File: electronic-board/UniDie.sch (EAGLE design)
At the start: 27 parts, among them IC1 ATMEGA88-THIN, J1 PJ-037A, J2 AVR_SPI_PROG_3X2NS

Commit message: Update on schematic and board.
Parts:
- removed R1, R10, R11, R13, R2, R3, R4, R6, R9: 120ohm, fab:RES-US1206FAB
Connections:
- removed net N$13: 7-SEG-LED2.5-DP, R6.2
- removed net N$2: 7-SEG-LED1.1-E, R3.2
- removed net N$3: 7-SEG-LED1.2-D, R4.2
- removed net N$4: 7-SEG-LED1.4-C, R1.2
- removed net N$5: 7-SEG-LED1.5-DP, R2.2
- removed net N$6: 7-SEG-LED1.10-G, R9.1
- removed net N$7: 7-SEG-LED1.9-F, R11.1
- removed net N$8: 7-SEG-LED1.7-A, R10.1
- removed net N$9: 7-SEG-LED1.6-B, R13.1
- removed net TA: R10.2
- removed net TB: R13.2
- removed net TC: R1.1
- removed net TD: R4.1
- removed net TDP: R2.1
- removed net TE: R3.1
- removed net TF: R11.2
- removed net TG: R9.2
- removed net UA: R16.2
- removed net UB: R17.2
- removed net UC: R5.1
- removed net UD: R8.1
- removed net UDP: R6.1
- removed net UE: R7.1
- removed net UF: R12.2
- removed net UG: R15.2
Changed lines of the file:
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@@
 <part name="SUPPLY5" library="SparkFun-PowerSymbols" deviceset="5V" device=""/>
 <part name="GND5" library="SparkFun-PowerSymbols" deviceset="GND" device=""/>
-<part name="R1" library="fab" deviceset="RES-US" device="1206FAB" value="120ohm"/>
-<part name="R2" library="fab" deviceset="RES-US" device="1206FAB" value="120ohm"/>
-<part name="R3" library="fab" deviceset="RES-US" device="1206FAB" value="120ohm"/>
-<part name="R4" library="fab" deviceset="RES-US" device="1206FAB" value="120ohm"/>
 <part name="R5" library="fab" deviceset="RES-US" device="1206FAB" value="120ohm"/>
-<part name="R6" library="fab" deviceset="RES-US" device="1206FAB" value="120ohm"/>
 <part name="R7" library="fab" deviceset="RES-US" device="1206FAB" value="120ohm"/>
 <part name="R8" library="fab" deviceset="RES-US" device="1206FAB" value="120ohm"/>
-<part name="R9" library="fab" deviceset="RES-US" device="1206FAB" value="120ohm"/>
-<part name="R10" library="fab" deviceset="RES-US" device="1206FAB" value="120ohm"/>
-<part name="R11" library="fab" deviceset="RES-US" device="1206FAB" value="120ohm"/>
 <part name="R12" library="fab" deviceset="RES-US" device="1206FAB" value="120ohm"/>
-<part name="R13" library="fab" deviceset="RES-US" device="1206FAB" value="120ohm"/>
 <part name="R15" library="fab" deviceset="RES-US" device="1206FAB" value="120ohm"/>
 <part name="R16" library="fab" deviceset="RES-US" device="1206FAB" value="120ohm"/>
@@
 <instance part="SUPPLY5" gate="G$1" x="78.74" y="40.64"/>
 <instance part="GND5" gate="1" x="190.5" y="5.08"/>
-<instance part="R1" gate="G$1" x="22.86" y="33.02"/>
-<instance part="R2" gate="G$1" x="22.86" y="25.4"/>
-<instance part="R3" gate="G$1" x="22.86" y="45.72"/>
-<instance part="R4" gate="G$1" x="22.86" y="38.1"/>
 <instance part="R5" gate="G$1" x="22.86" y="2.54"/>
-<instance part="R6" gate="G$1" x="22.86" y="-5.08"/>
 <instance part="R7" gate="G$1" x="22.86" y="15.24"/>
 <instance part="R8" gate="G$1" x="22.86" y="7.62"/>
-<instance part="R9" gate="G$1" x="63.5" y="45.72"/>
-<instance part="R10" gate="G$1" x="63.5" y="33.02"/>
-<instance part="R11" gate="G$1" x="63.5" y="38.1"/>
 <instance part="R12" gate="G$1" x="63.5" y="7.62"/>
-<instance part="R13" gate="G$1" x="63.5" y="25.4"/>
 <instance part="R15" gate="G$1" x="63.5" y="15.24"/>
 <instance part="R16" gate="G$1" x="63.5" y="2.54"/>
@@
 </segment>
 </net>
-<net name="N$2" class="0">
-<segment>
-<pinref part="R3" gate="G$1" pin="2"/>
-<wire x1="27.94" y1="45.72" x2="30.48" y2="45.72" width="0.1524" layer="91"/>
-<wire x1="30.48" y1="45.72" x2="30.48" y2="40.64" width="0.1524" layer="91"/>
-<pinref part="7-SEG-LED1" gate="G$1" pin="1-E"/>
-<wire x1="30.48" y1="40.64" x2="33.02" y2="40.64" width="0.1524" layer="91"/>
-</segment>
-</net>
-<net name="N$3" class="0">
-<segment>
-<pinref part="7-SEG-LED1" gate="G$1" pin="2-D"/>
-<pinref part="R4" gate="G$1" pin="2"/>
-<wire x1="33.02" y1="38.1" x2="27.94" y2="38.1" width="0.1524" layer="91"/>
-</segment>
-</net>
-<net name="N$4" class="0">
-<segment>
-<pinref part="7-SEG-LED1" gate="G$1" pin="4-C"/>
-<pinref part="R1" gate="G$1" pin="2"/>
-<wire x1="33.02" y1="33.02" x2="27.94" y2="33.02" width="0.1524" layer="91"/>
-</segment>
-</net>
-<net name="N$5" class="0">
-<segment>
-<pinref part="7-SEG-LED1" gate="G$1" pin="5-DP"/>
-<wire x1="33.02" y1="30.48" x2="30.48" y2="30.48" width="0.1524" layer="91"/>
-<wire x1="30.48" y1="30.48" x2="30.48" y2="25.4" width="0.1524" layer="91"/>
-<pinref part="R2" gate="G$1" pin="2"/>
-<wire x1="30.48" y1="25.4" x2="27.94" y2="25.4" width="0.1524" layer="91"/>
-</segment>
-</net>
-<net name="N$6" class="0">
-<segment>
-<pinref part="7-SEG-LED1" gate="G$1" pin="10-G"/>
-<wire x1="53.34" y1="40.64" x2="55.88" y2="40.64" width="0.1524" layer="91"/>
-<wire x1="55.88" y1="40.64" x2="55.88" y2="45.72" width="0.1524" layer="91"/>
-<pinref part="R9" gate="G$1" pin="1"/>
-<wire x1="55.88" y1="45.72" x2="58.42" y2="45.72" width="0.1524" layer="91"/>
-</segment>
-</net>
-<net name="N$7" class="0">
-<segment>
-<pinref part="7-SEG-LED1" gate="G$1" pin="9-F"/>
-<pinref part="R11" gate="G$1" pin="1"/>
-<wire x1="53.34" y1="38.1" x2="58.42" y2="38.1" width="0.1524" layer="91"/>
-</segment>
-</net>
-<net name="N$8" class="0">
-<segment>
-<pinref part="7-SEG-LED1" gate="G$1" pin="7-A"/>
-<pinref part="R10" gate="G$1" pin="1"/>
-<wire x1="53.34" y1="33.02" x2="58.42" y2="33.02" width="0.1524" layer="91"/>
-</segment>
-</net>
-<net name="N$9" class="0">
-<segment>
-<pinref part="7-SEG-LED1" gate="G$1" pin="6-B"/>
-<wire x1="53.34" y1="30.48" x2="55.88" y2="30.48" width="0.1524" layer="91"/>
-<wire x1="55.88" y1="30.48" x2="55.88" y2="25.4" width="0.1524" layer="91"/>
-<pinref part="R13" gate="G$1" pin="1"/>
-<wire x1="55.88" y1="25.4" x2="58.42" y2="25.4" width="0.1524" layer="91"/>
-</segment>
-</net>
 <net name="N$10" class="0">
 <segment>
@@
 </segment>
 </net>
-<net name="N$13" class="0">
-<segment>
-<pinref part="7-SEG-LED2" gate="G$1" pin="5-DP"/>
-<wire x1="33.02" y1="0" x2="30.48" y2="0" width="0.1524" layer="91"/>
-<wire x1="30.48" y1="0" x2="30.48" y2="-2.54" width="0.1524" layer="91"/>
-<pinref part="R6" gate="G$1" pin="2"/>
-<wire x1="30.48" y1="-2.54" x2="30.48" y2="-5.08" width="0.1524" layer="91"/>
-<wire x1="30.48" y1="-5.08" x2="27.94" y2="-5.08" width="0.1524" layer="91"/>
-</segment>
-</net>
-<net name="TE" class="0">
-<segment>
-<pinref part="R3" gate="G$1" pin="1"/>
-<wire x1="17.78" y1="45.72" x2="15.24" y2="45.72" width="0.1524" layer="91"/>
-<label x="15.24" y="48.26" size="1.778" layer="95" rot="R180"/>
-</segment>
-</net>
-<net name="TD" class="0">
-<segment>
-<pinref part="R4" gate="G$1" pin="1"/>
-<wire x1="17.78" y1="38.1" x2="15.24" y2="38.1" width="0.1524" layer="91"/>
-<label x="15.24" y="40.64" size="1.778" layer="95" rot="R180"/>
-</segment>
-</net>
-<net name="TC" class="0">
-<segment>
-<pinref part="R1" gate="G$1" pin="1"/>
-<wire x1="17.78" y1="33.02" x2="15.24" y2="33.02" width="0.1524" layer="91"/>
-<label x="15.24" y="35.56" size="1.778" layer="95" rot="R180"/>
-</segment>
-</net>
-<net name="TDP" class="0">
-<segment>
-<pinref part="R2" gate="G$1" pin="1"/>
-<wire x1="17.78" y1="25.4" x2="15.24" y2="25.4" width="0.1524" layer="91"/>
-<label x="15.24" y="27.94" size="1.778" layer="95" rot="R180"/>
-</segment>
-</net>
-<net name="TG" class="0">
-<segment>
-<pinref part="R9" gate="G$1" pin="2"/>
-<wire x1="68.58" y1="45.72" x2="71.12" y2="45.72" width="0.1524" layer="91"/>
-<label x="71.12" y="45.72" size="1.778" layer="95"/>
-</segment>
-</net>
-<net name="TF" class="0">
-<segment>
-<pinref part="R11" gate="G$1" pin="2"/>
-<wire x1="68.58" y1="38.1" x2="71.12" y2="38.1" width="0.1524" layer="91"/>
-<label x="71.12" y="38.1" size="1.778" layer="95"/>
-</segment>
-</net>
-<net name="TA" class="0">
-<segment>
-<pinref part="R10" gate="G$1" pin="2"/>
-<wire x1="68.58" y1="33.02" x2="71.12" y2="33.02" width="0.1524" layer="91"/>
-<label x="71.12" y="33.02" size="1.778" layer="95"/>
-</segment>
-</net>
-<net name="TB" class="0">
-<segment>
-<pinref part="R13" gate="G$1" pin="2"/>
-<wire x1="68.58" y1="25.4" x2="71.12" y2="25.4" width="0.1524" layer="91"/>
-<label x="71.12" y="25.4" size="1.778" layer="95"/>
-</segment>
-</net>
-<net name="UE" class="0">
-<segment>
-<pinref part="R7" gate="G$1" pin="1"/>
-<wire x1="17.78" y1="15.24" x2="15.24" y2="15.24" width="0.1524" layer="91"/>
-<label x="15.24" y="17.78" size="1.778" layer="95" rot="R180"/>
-</segment>
-</net>
-<net name="UD" class="0">
-<segment>
-<pinref part="R8" gate="G$1" pin="1"/>
-<wire x1="17.78" y1="7.62" x2="15.24" y2="7.62" width="0.1524" layer="91"/>
-<label x="15.24" y="10.16" size="1.778" layer="95" rot="R180"/>
-</segment>
-</net>
-<net name="UC" class="0">
-<segment>
-<pinref part="R5" gate="G$1" pin="1"/>
-<wire x1="17.78" y1="2.54" x2="15.24" y2="2.54" width="0.1524" layer="91"/>
-<label x="15.24" y="5.08" size="1.778" layer="95" rot="R180"/>
-</segment>
-</net>
-<net name="UDP" class="0">
-<segment>
-<pinref part="R6" gate="G$1" pin="1"/>
-<wire x1="17.78" y1="-5.08" x2="15.24" y2="-5.08" width="0.1524" layer="91"/>
-<label x="15.24" y="-2.54" size="1.778" layer="95" rot="R180"/>
-</segment>
-</net>
-<net name="UG" class="0">
-<segment>
-<pinref part="R15" gate="G$1" pin="2"/>
-<wire x1="68.58" y1="15.24" x2="71.12" y2="15.24" width="0.1524" layer="91"/>
-<label x="71.12" y="15.24" size="1.778" layer="95"/>
-</segment>
-</net>
 <net name="N$27" class="0">
 <segment>
@@
 </segment>
 </net>
-<net name="UF" class="0">
-<segment>
-<pinref part="R12" gate="G$1" pin="2"/>
-<wire x1="68.58" y1="7.62" x2="71.12" y2="7.62" width="0.1524" layer="91"/>
-<label x="71.12" y="7.62" size="1.778" layer="95"/>
-</segment>
-</net>
-<net name="UA" class="0">
-<segment>
-<pinref part="R16" gate="G$1" pin="2"/>
-<wire x1="68.58" y1="2.54" x2="71.12" y2="2.54" width="0.1524" layer="91"/>
-<label x="71.12" y="2.54" size="1.778" layer="95"/>
-</segment>
-</net>
-<net name="UB" class="0">
-<segment>
-<pinref part="R17" gate="G$1" pin="2"/>
-<wire x1="68.58" y1="-5.08" x2="71.12" y2="-5.08" width="0.1524" layer="91"/>
-<label x="71.12" y="-5.08" size="1.778" layer="95"/>
-</segment>
-</net>

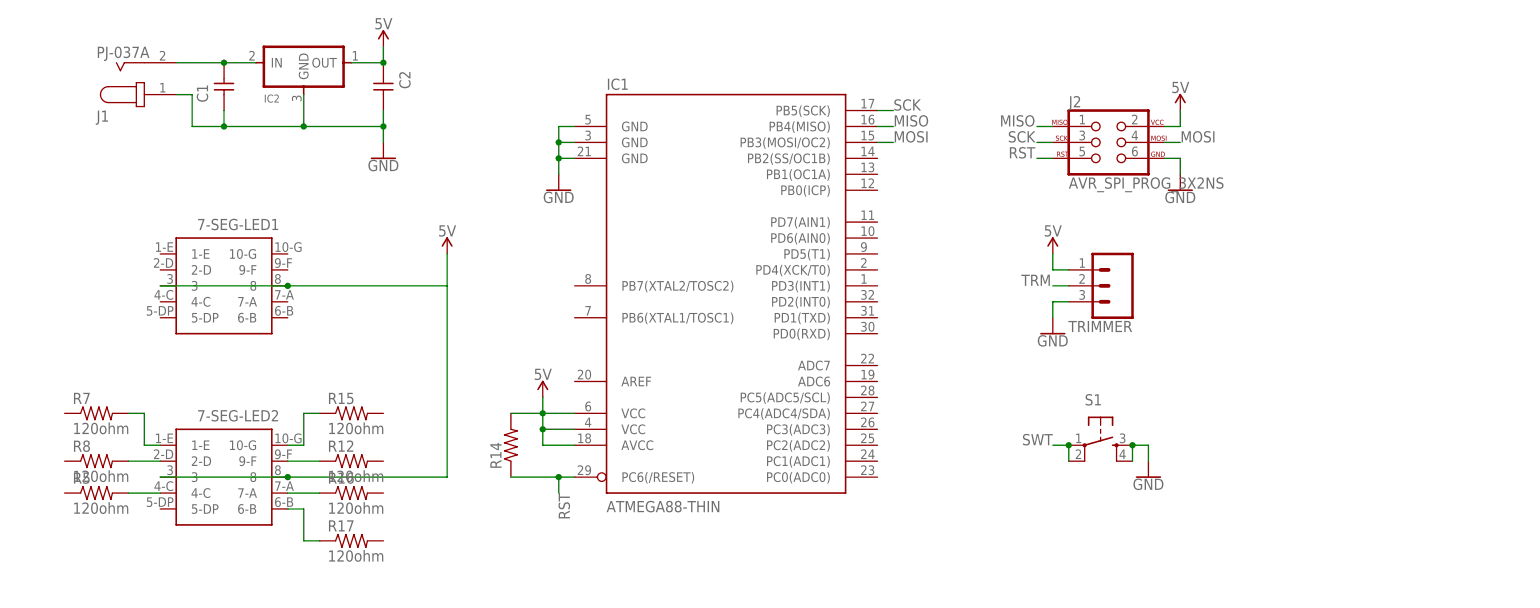
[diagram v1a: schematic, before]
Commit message: Finished schematic and approximate board layout. Updated electronics BOM
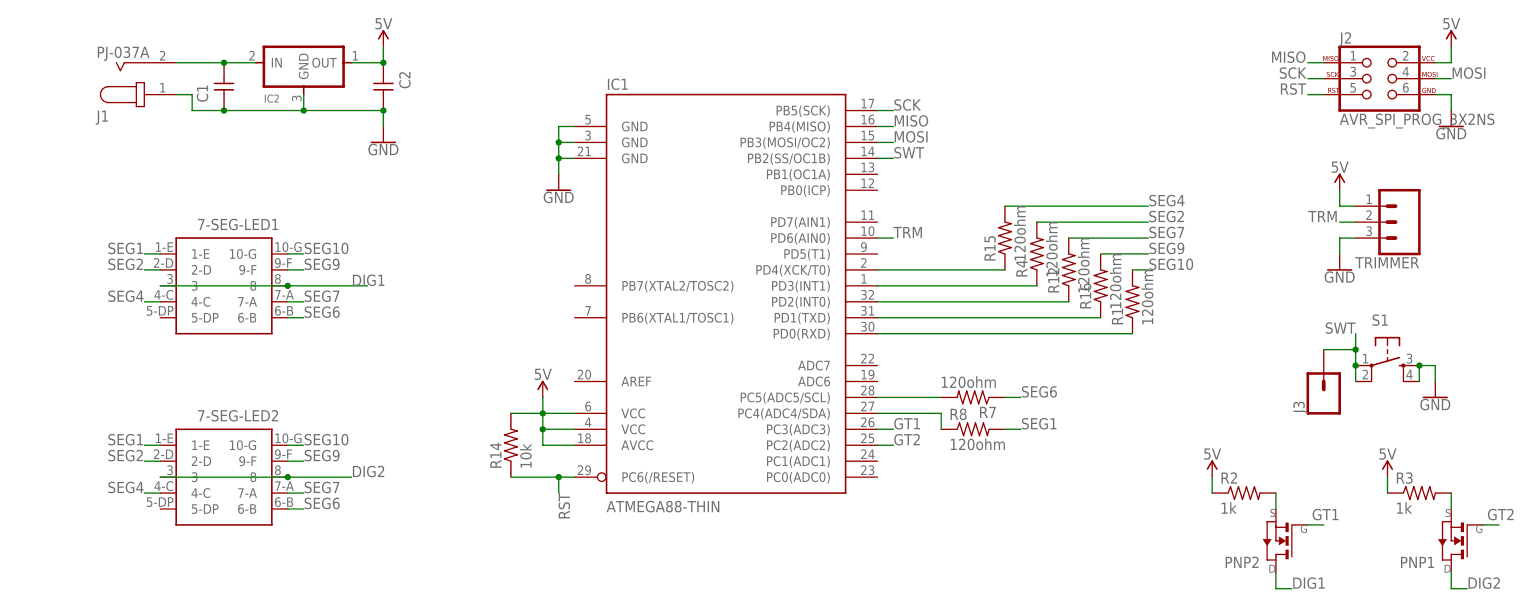
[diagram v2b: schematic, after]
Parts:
- removed R17, R5: 120ohm, fab:RES-US1206FAB
- added J3: (no value), SparkFun-Connectors:CONN_01PTH_NO_SILK_YES_STOP
- added PNP1, PNP2: (no value), fab:NMOSFETSOT23
- added R1, R4: 120ohm, fab:RES-US1206FAB
- added R2, R3: 1k, fab:RES-US1206FAB
- R14: value (none) -> 10k
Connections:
- removed net N$11: 7-SEG-LED2.2-D, R8.2
- removed net N$12: 7-SEG-LED2.4-C, R5.2
- removed net N$27: 7-SEG-LED2.10-G, R15.1
- removed net N$28: 7-SEG-LED2.9-F, R12.1
- removed net N$29: 7-SEG-LED2.7-A, R16.1
- removed net N$30: 7-SEG-LED2.6-B, R17.1
- new net DIG1: 7-SEG-LED1.3, 7-SEG-LED1.8, PNP2.D
- new net DIG2: 7-SEG-LED2.3, 7-SEG-LED2.8, PNP1.D
- new net GT1: IC1.PC3(ADC3), PNP2.G
- new net GT2: IC1.PC2(ADC2), PNP1.G
- new net N$13: PNP2.S, R2.2
- new net N$2: PNP1.S, R3.2
- new net N$3: IC1.PC5(ADC5/SCL), R7.2
- new net N$4: IC1.PC4(ADC4/SDA), R8.1
- new net N$6: IC1.PD4(XCK/T0), R15.1
- new net N$7: IC1.PD3(INT1), R4.1
- new net N$8: IC1.PD2(INT0), R12.1
- new net N$9: IC1.PD1(TXD), R16.1
- new net SEG1: 7-SEG-LED1.1-E, 7-SEG-LED2.1-E, R8.2
- new net SEG10: 7-SEG-LED1.10-G, 7-SEG-LED2.10-G, R1.2
- new net SEG2: 7-SEG-LED1.2-D, 7-SEG-LED2.2-D, R4.2
- new net SEG4: 7-SEG-LED1.4-C, 7-SEG-LED2.4-C, R15.2
- new net SEG6: 7-SEG-LED1.6-B, 7-SEG-LED2.6-B, R7.1
- new net SEG7: 7-SEG-LED1.7-A, 7-SEG-LED2.7-A, R12.2
- new net SEG9: 7-SEG-LED1.9-F, 7-SEG-LED2.9-F, R16.2
- net 5V: now also R2.1, R3.1; no longer 7-SEG-LED1.3, 7-SEG-LED1.8, 7-SEG-LED2.3, 7-SEG-LED2.8
- net N$10: now also IC1.PD0(RXD), R1.1; no longer 7-SEG-LED2.1-E, R7.2
- net SWT: now also IC1.PB2(SS/OC1B), J3.1
- net TRM: now also IC1.PD6(AIN0)
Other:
- moved on the sheet: J2, R12, R15, R16, R7, R8, S1, TRIMMER

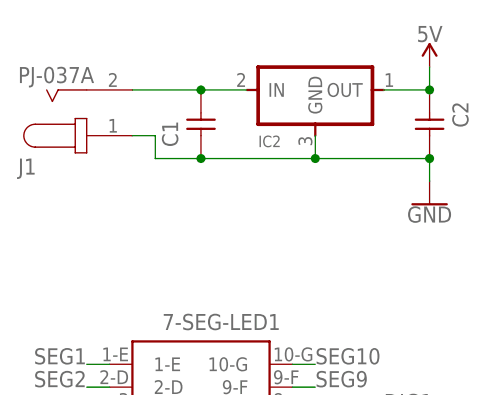
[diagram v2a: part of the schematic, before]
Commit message: Updated dxf layout on board. Removed dc plug and added power pins. Added holes to board
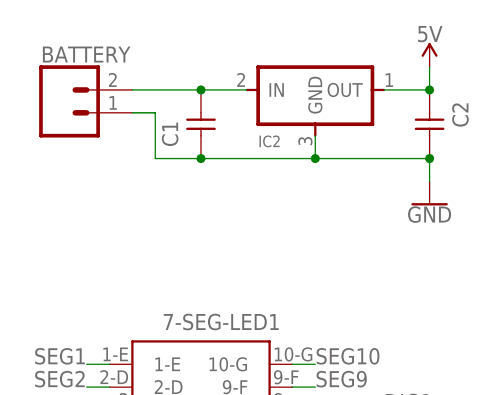
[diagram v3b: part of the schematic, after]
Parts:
- removed J1: PJ-037A, PJ-037A:PJ-037A
- added BATTERY: (no value), SparkFun-Connectors:CONN_021X02_NO_SILK
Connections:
- net GND: now also BATTERY.1; no longer J1.1
- net N$1: now also BATTERY.2; no longer J1.2
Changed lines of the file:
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@@
 <part name="S1" library="fab" deviceset="6MM_SWITCH" device="6MM_SWITCH"/>
 <part name="IC2" library="fab" deviceset="REGULATOR" device="SOT23"/>
-<part name="J1" library="PJ-037A" deviceset="PJ-037A" device=""/>
 <part name="J2" library="SparkFun-Connectors" deviceset="AVR_SPI_PROG_3X2" device="NS"/>
 <part name="TRIMMER" library="SparkFun-Connectors" deviceset="CONN_03" device="1X03_NO_SILK"/>
@@
 <part name="R4" library="fab" deviceset="RES-US" device="1206FAB" value="120ohm"/>
 <part name="J3" library="SparkFun-Connectors" deviceset="CONN_01" device="PTH_NO_SILK_YES_STOP"/>
+<part name="BATTERY" library="SparkFun-Connectors" deviceset="CONN_02" device="1X02_NO_SILK"/>
 </parts>
 <sheets>
@@
 <instance part="S1" gate="2" x="228.6" y="22.86" rot="R270"/>
 <instance part="IC2" gate="G$1" x="55.88" y="68.58"/>
-<instance part="J1" gate="G$1" x="30.48" y="68.58" rot="MR180"/>
 <instance part="J2" gate="G$1" x="226.06" y="68.58"/>
 <instance part="TRIMMER" gate="J$1" x="231.14" y="45.72" rot="R180"/>
@@
 <instance part="R4" gate="G$1" x="172.72" y="40.64" rot="R90"/>
 <instance part="J3" gate="G$1" x="218.44" y="17.78" rot="R90"/>
+<instance part="BATTERY" gate="G$1" x="27.94" y="68.58"/>
 </instances>
 <busses>
@@
 <net name="N$1" class="0">
 <segment>
-<pinref part="J1" gate="G$1" pin="2"/>
 <pinref part="C1" gate="&gt;NAME" pin="2"/>
 <wire x1="35.56" y1="71.12" x2="43.18" y2="71.12" width="0.1524" layer="91"/>
@@
 <wire x1="48.26" y1="71.12" x2="43.18" y2="71.12" width="0.1524" layer="91"/>
 <junction x="43.18" y="71.12"/>
+<pinref part="BATTERY" gate="G$1" pin="2"/>
 </segment>
 </net>
@@
 <pinref part="C1" gate="&gt;NAME" pin="1"/>
 <wire x1="43.18" y1="63.5" x2="38.1" y2="63.5" width="0.1524" layer="91"/>
-<wire x1="38.1" y1="63.5" x2="38.1" y2="66.04" width="0.1524" layer="91"/>
-<pinref part="J1" gate="G$1" pin="1"/>
-<wire x1="38.1" y1="66.04" x2="35.56" y2="66.04" width="0.1524" layer="91"/>
+<wire x1="38.1" y1="63.5" x2="38.1" y2="68.58" width="0.1524" layer="91"/>
+<wire x1="38.1" y1="68.58" x2="35.56" y2="68.58" width="0.1524" layer="91"/>
 <pinref part="IC2" gate="G$1" pin="GND"/>
 <wire x1="55.88" y1="66.04" x2="55.88" y2="63.5" width="0.1524" layer="91"/>
@@
 <wire x1="68.58" y1="63.5" x2="68.58" y2="60.96" width="0.1524" layer="91"/>
 <junction x="68.58" y="63.5"/>
+<pinref part="BATTERY" gate="G$1" pin="1"/>
 </segment>
 <segment>
